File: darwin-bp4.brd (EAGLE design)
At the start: 110 x 127.9 mm, 11 parts

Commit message: Panelization. Production Articles 1 and 2.
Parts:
- moved R1 20.9 mm to (51.1, 108.8)
- moved R2 20.9 mm to (45.3, 108.8)
- moved R3 20.9 mm to (89.2, 72.5)
- moved R4 20.9 mm to (78.1, 70.2)
- moved U$1 20.9 mm to (86.8, 64.1)
- moved U$13 20.9 mm to (47.0, 123.7)
- moved U$2 20.9 mm to (17.5, 103.0)
- moved U$3 20.9 mm to (17.5, 77.0)
- moved U$4 20.9 mm to (17.5, 51.0)
- moved U$5 20.9 mm to (17.5, 25.0)
- moved U$6 20.9 mm to (74.5, 64.0)
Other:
- board size 110 x 127.9 mm -> 95 x 128 mm

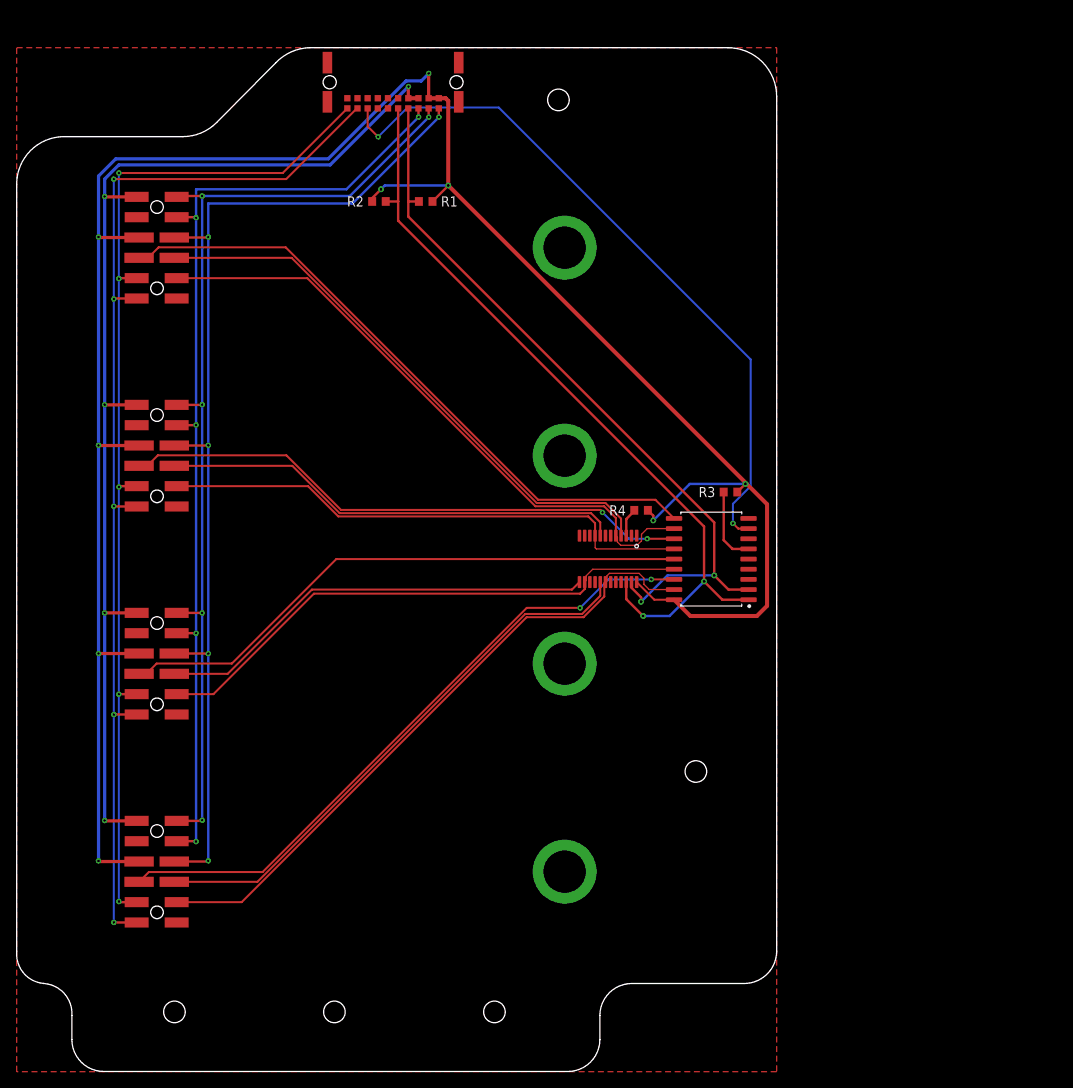
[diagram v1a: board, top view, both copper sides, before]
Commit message: Added LEDs and decoupling.
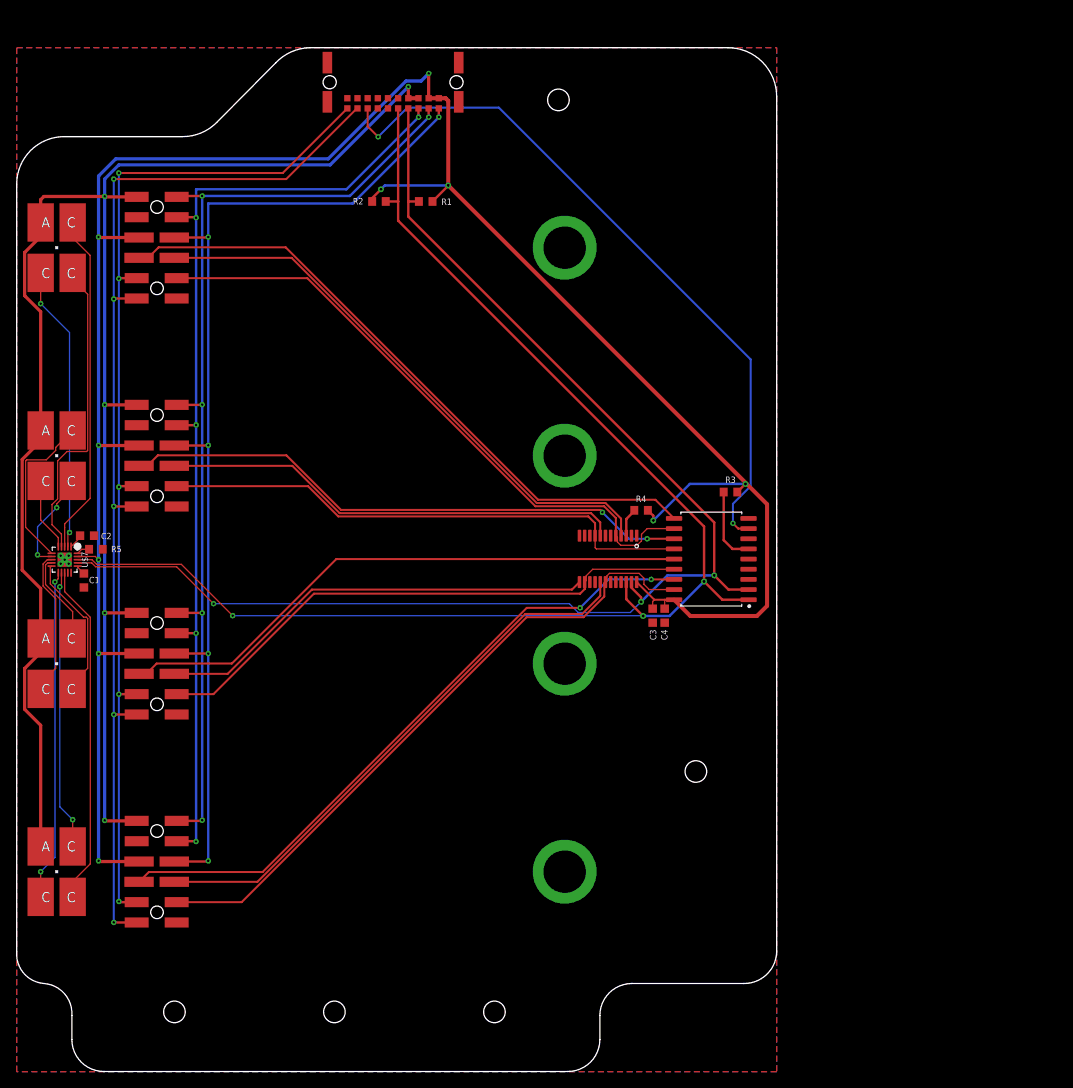
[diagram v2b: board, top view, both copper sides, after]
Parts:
- added C1: .1u, rcl:C0603K
- added C2, C3, C4: 1u, rcl:C0603K
- added LED1, LED2, LED3, LED4: (no value), led:P-LCC-4
- added R5: (no value), rcl:R0603
- added U$7: LP5012, Conservify:QFN40P300X300X80-20N
- R1, R2: value (none) -> 4.7k
- R3, R4: value (none) -> 10k
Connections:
- new net N$1: LED1.C@1, U$7.2
- new net N$11: LED3.C@4, U$7.10
- new net N$12: LED4.C@1, U$7.11
- new net N$13: LED4.C@3, U$7.12
- new net N$14: LED4.C@4, U$7.13
- new net N$20: C2.2, U$7.1
- new net N$21: R5.1, U$7.20
- new net N$3: LED1.C@3, U$7.3
- new net N$4: LED1.C@4, U$7.4
- new net N$5: LED2.C@1, U$7.5
- new net N$6: LED2.C@3, U$7.6
- new net N$7: LED2.C@4, U$7.7
- new net N$8: LED3.C@1, U$7.8
- new net N$9: LED3.C@3, U$7.9
- net 3V3: now also C1.2, C3.2, C4.2, U$7.16, U$7.19
- net GND: now also C1.1, C2.1, C3.1, C4.1, R5.2, U$7.14, U$7.15, U$7.P$1, U$7.P$2, U$7.P$3, U$7.P$4, U$7.P$5, U$7.P$6
- net MOD_SCL: now also U$7.18
- net MOD_SDA: now also U$7.17
- net UNREG: now also LED1.A, LED2.A, LED3.A, LED4.A
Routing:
- net UNREG: track 141.7 -> 236.0 mm
- net MOD_SCL: track 97.5 -> 171.1 mm, vias 2 -> 3
- net MOD_SDA: track 94.0 -> 167.6 mm, vias 2 -> 3
- net N$14: track 0.00 -> 42.8 mm
- net N$3: track 0.00 -> 42.7 mm
- net N$12: track 0.00 -> 41.4 mm, vias 0 -> 2
- net N$4: track 0.00 -> 38.8 mm
- net N$1: track 0.00 -> 35.8 mm, vias 0 -> 2
- net N$13: track 0.00 -> 35.0 mm, vias 0 -> 2
- net N$6: track 0.00 -> 20.6 mm
- net N$11: track 0.00 -> 18.3 mm
- net N$8: track 0.00 -> 18.3 mm
- net N$7: track 0.00 -> 12.9 mm, vias 0 -> 2
- net N$9: track 0.00 -> 11.5 mm
- net N$5: track 0.00 -> 9.13 mm
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- added copper zone on layer 16, net GND

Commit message: Cleanup.
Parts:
- C3, C4: value 1u -> .1uf
- renumbered U$1 to U1, U$13 to MEZZ-TO-RADIO, U$2 to SLOT1, U$3 to SLOT2, U$4 to SLOT3, U$5 to SLOT4, U$6 to U2, U$7 to U3

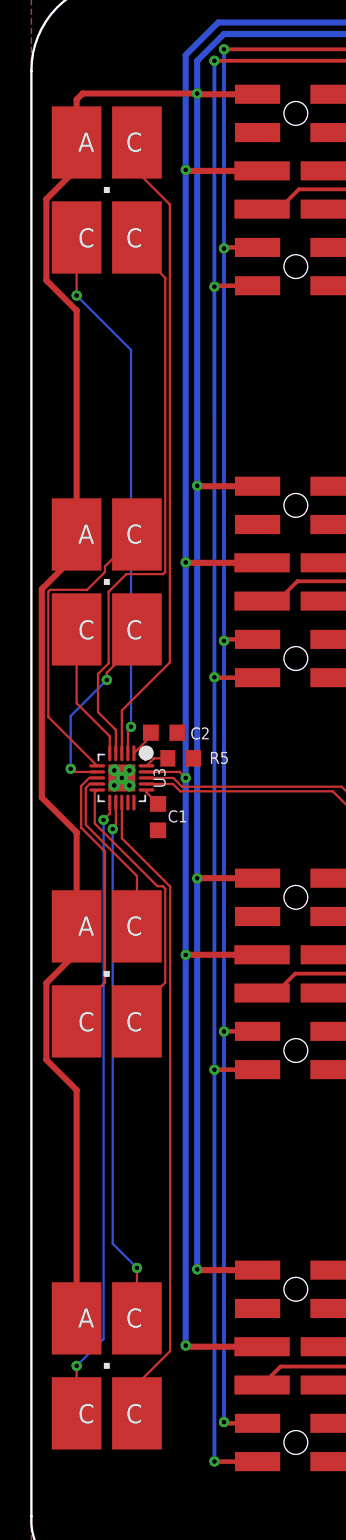
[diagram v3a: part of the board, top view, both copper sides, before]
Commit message: Fixed LED footprints and tidied routing.
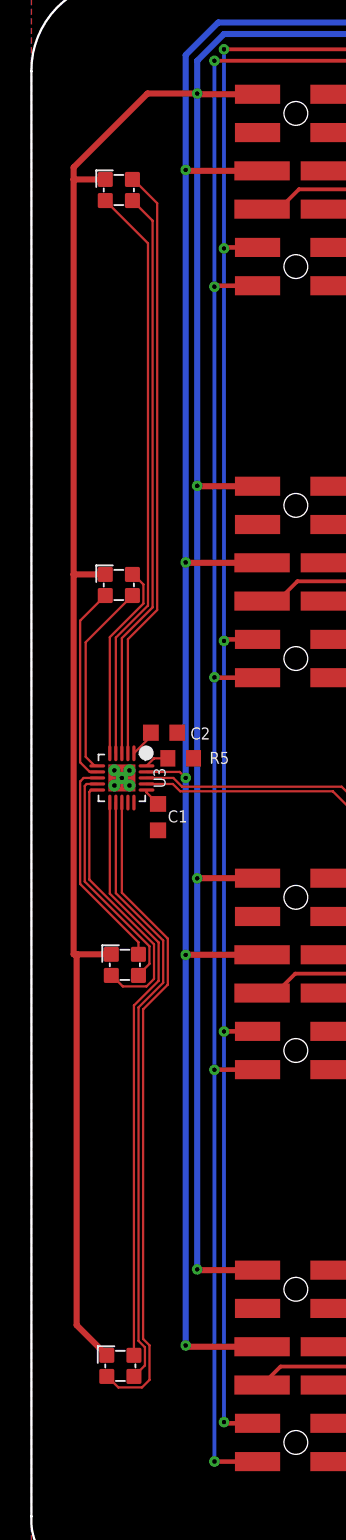
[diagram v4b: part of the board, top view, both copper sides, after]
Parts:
- removed LED1, LED2, LED3, LED4: (no value), led:P-LCC-4
- added U$1, U$2, U$3, U$4: CLMVC-FKC-CGJJM569ABB7A343, Conservify:2MMPLCC4
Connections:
- net N$1: now also U$1.C3; no longer LED1.C@1
- net N$11: now also U$3.C1; no longer LED3.C@4
- net N$12: now also U$4.C3; no longer LED4.C@1
- net N$13: now also U$4.C2; no longer LED4.C@3
- net N$14: now also U$4.C1; no longer LED4.C@4
- net N$3: now also U$1.C2; no longer LED1.C@3
- net N$4: now also U$1.C1; no longer LED1.C@4
- net N$5: now also U$2.C3; no longer LED2.C@1
- net N$6: now also U$2.C2; no longer LED2.C@3
- net N$7: now also U$2.C1; no longer LED2.C@4
- net N$8: now also U$3.C3; no longer LED3.C@1
- net N$9: now also U$3.C2; no longer LED3.C@3
- net UNREG: now also U$1.A, U$2.A, U$3.A, U$4.A; no longer LED1.A, LED2.A, LED3.A, LED4.A
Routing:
- net N$6: track 20.6 -> 13.0 mm
- net N$13: track 35.0 -> 40.5 mm, vias 2 -> 0
- net N$3: track 42.7 -> 38.1 mm
- net N$9: track 11.5 -> 15.5 mm
- net N$8: track 18.3 -> 14.3 mm
- net N$5: track 9.13 -> 13.1 mm
- net N$1: track 35.8 -> 39.6 mm, vias 2 -> 0
- net N$12: track 41.4 -> 38.7 mm, vias 2 -> 0
- net UNREG: track 236.0 -> 238.3 mm
- net N$14: track 42.8 -> 43.8 mm
- net N$7: track 12.9 -> 13.2 mm, vias 2 -> 0
